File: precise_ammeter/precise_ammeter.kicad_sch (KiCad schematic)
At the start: 0 parts

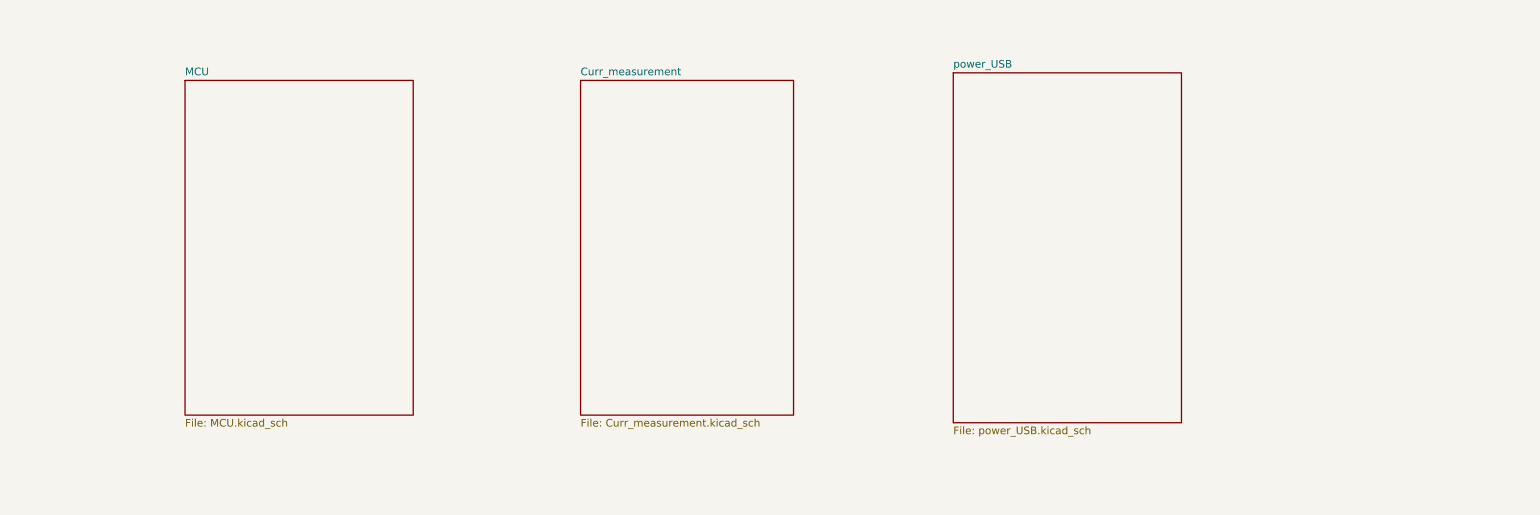
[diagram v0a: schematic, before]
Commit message: Dodano schemat frontend_1
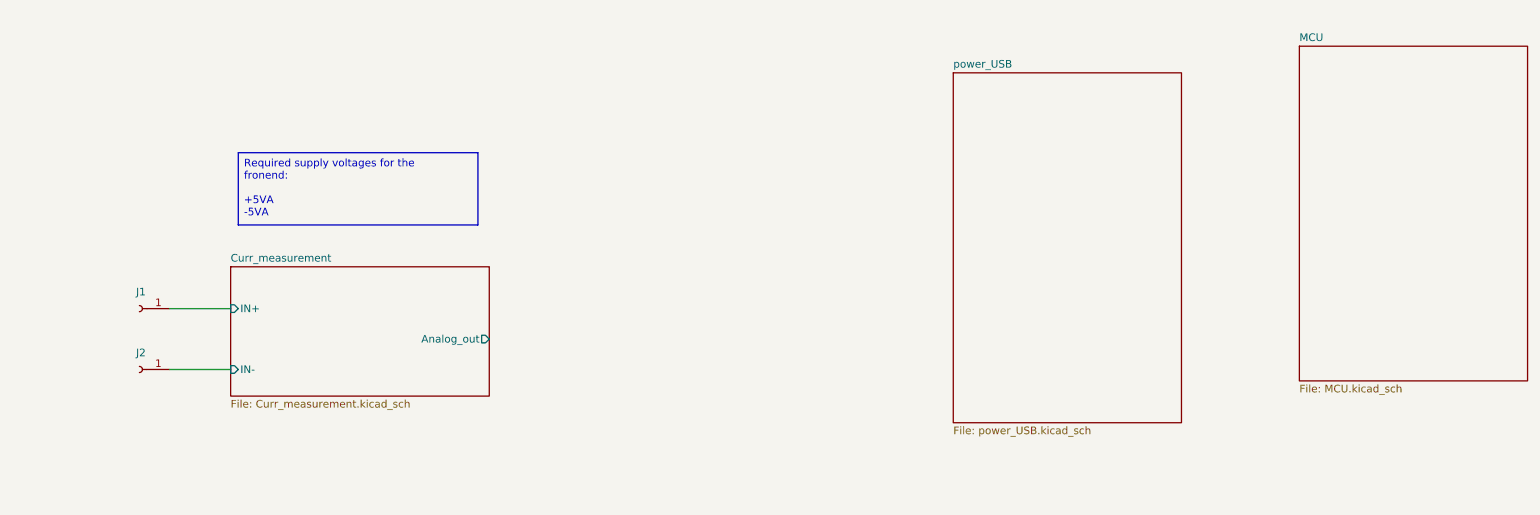
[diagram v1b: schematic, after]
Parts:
- added J1, J2: Conn_01x01_Socket, Connector:Banana_Jack_1Pin, symbol Connector:Conn_01x01_Socket
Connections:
- new net Curr_measurement/IN+: J1.1 (Pin_1)
- new net Curr_measurement/IN-: J2.1 (Pin_1)
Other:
- sheet Curr_measurement ports: added Analog_out, IN+, IN-; removed none
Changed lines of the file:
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@@
 	(generator_version "9.0")
 	(paper "A4")
+	(text_box "Required supply voltages for the fronend:\n\n+5VA\n-5VA"
+		(exclude_from_sim no)
+		(at 57.15 67.945 0)
+		(size 40.005 12.065)
+		(margins 0.9525 0.9525 0.9525 0.9525)
+		(stroke
+			(width 0)
+			(type solid)
+		)
+		(fill
+			(type none)
+		)
+		(effects
+			(font
+				(size 1.27 1.27)
+			)
+			(justify left top)
+		)
+	)
+	(wire
+		(pts
+			(xy 45.72 93.98) (xy 55.88 93.98)
+		)
+		(stroke
+			(width 0)
+			(type default)
+		)
+	)
+	(wire
+		(pts
+			(xy 45.72 104.14) (xy 55.88 104.14)
+		)
+		(stroke
+			(width 0)
+			(type default)
+		)
+	)
+	(symbol
+		(lib_id "Connector:Conn_01x01_Socket")
+		(at 40.64 93.98 180)
+		(unit 1)
+		(exclude_from_sim no)
+		(in_bom yes)
+		(on_board yes)
+		(dnp no)
+		(property "Reference" "J1"
+			(at 40.894 91.186 0)
+			(effects
+				(font
+					(size 1.27 1.27)
+				)
+			)
+		)
+		(property "Value" "Conn_01x01_Socket"
+			(at 41.275 91.44 0)
+			(effects
+				(font
+					(size 1.27 1.27)
+				)
+				(hide yes)
+			)
+		)
+		(property "Footprint" "Connector:Banana_Jack_1Pin"
+			(at 40.64 93.98 0)
+			(effects
+				(font
+					(size 1.27 1.27)
+				)
+				(hide yes)
+			)
+		)
+		(property "Datasheet" "~"
+			(at 40.64 93.98 0)
+			(effects
+				(font
+					(size 1.27 1.27)
+				)
+				(hide yes)
+			)
+		)
+		(property "Description" "Generic connector, single row, 01x01, script generated"
+			(at 40.64 93.98 0)
+			(effects
+				(font
+					(size 1.27 1.27)
+				)
+				(hide yes)
+			)
+		)
+		(pin "1"
+		)
+		(instances
+			(project ""
+				(path "/7da3b652-85ac-4caa-8d8d-9cad461e9c85"
+					(reference "J1")
+					(unit 1)
+				)
+			)
+		)
+	)
+	(symbol
+		(lib_id "Connector:Conn_01x01_Socket")
+		(at 40.64 104.14 180)
+		(unit 1)
+		(exclude_from_sim no)
+		(in_bom yes)
+		(on_board yes)
+		(dnp no)
+		(property "Reference" "J2"
+			(at 40.894 101.346 0)
+			(effects
+				(font
+					(size 1.27 1.27)
+				)
+			)
+		)
+		(property "Value" "Conn_01x01_Socket"
+			(at 41.275 101.6 0)
+			(effects
+				(font
+					(size 1.27 1.27)
+				)
+				(hide yes)
+			)
+		)
+		(property "Footprint" "Connector:Banana_Jack_1Pin"
+			(at 40.64 104.14 0)
+			(effects
+				(font
+					(size 1.27 1.27)
+				)
+				(hide yes)
+			)
+		)
+		(property "Datasheet" "~"
+			(at 40.64 104.14 0)
+			(effects
+				(font
+					(size 1.27 1.27)
+				)
+				(hide yes)
+			)
+		)
+		(property "Description" "Generic connector, single row, 01x01, script generated"
+			(at 40.64 104.14 0)
+			(effects
+				(font
+					(size 1.27 1.27)
+				)
+				(hide yes)
+			)
+		)
+		(pin "1"
+		)
+		(instances
+			(project "precise_ammeter"
+				(path "/7da3b652-85ac-4caa-8d8d-9cad461e9c85"
+					(reference "J2")
+					(unit 1)
+				)
+			)
+		)
+	)
 	(sheet
-		(at 48.26 55.88)
+		(at 234.315 50.165)
 		(size 38.1 55.88)
 		(exclude_from_sim no)
@@
 		)
 		(property "Sheetname" "MCU"
-			(at 48.26 55.1684 0)
+			(at 234.315 49.4534 0)
 			(effects
 				(font
@@
 		)
 		(property "Sheetfile" "MCU.kicad_sch"
-			(at 48.26 112.3446 0)
+			(at 234.315 106.6296 0)
 			(effects
 				(font
@@
 	)
 	(sheet
-		(at 114.3 55.88)
-		(size 35.56 55.88)
+		(at 55.88 86.995)
+		(size 43.18 21.59)
 		(exclude_from_sim no)
 		(in_bom yes)
@@
 		)
 		(property "Sheetname" "Curr_measurement"
-			(at 114.3 55.1684 0)
+			(at 55.88 86.2834 0)
 			(effects
 				(font
@@
 		)
 		(property "Sheetfile" "Curr_measurement.kicad_sch"
-			(at 114.3 112.3446 0)
+			(at 55.88 109.1696 0)
 			(effects
 				(font
@@
 			)
 		)
+		(pin "Analog_out" output
+			(at 99.06 99.06 0)
+			(effects
+				(font
+					(size 1.27 1.27)
+				)
+				(justify right)
+			)
+		)
+		(pin "IN+" input
+			(at 55.88 93.98 180)
+			(effects
+				(font
+					(size 1.27 1.27)
+				)
+				(justify left)
+			)
+		)
+		(pin "IN-" input
+			(at 55.88 104.14 180)
+			(effects
+				(font
+					(size 1.27 1.27)
+				)
+				(justify left)
+			)
+		)

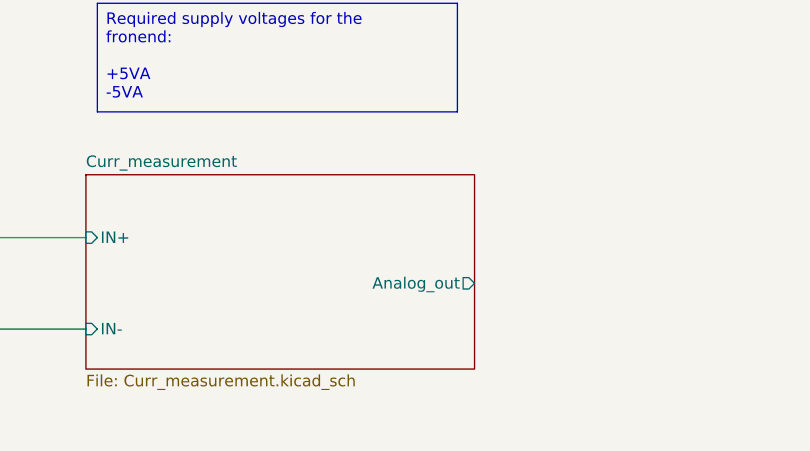
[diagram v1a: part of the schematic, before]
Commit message: Dodano drugi schemat frontendu
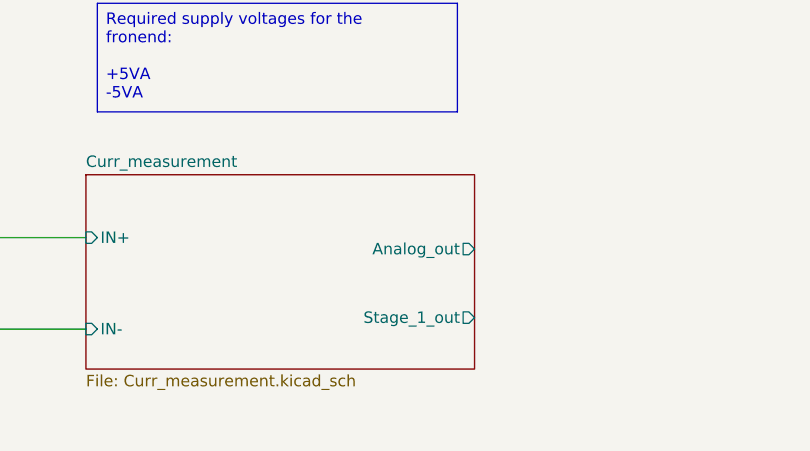
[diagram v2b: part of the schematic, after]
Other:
- sheet Curr_measurement ports: added Stage_1_out; removed none
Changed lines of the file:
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@@
 		)
 		(pin "Analog_out" output
-			(at 99.06 99.06 0)
+			(at 99.06 95.25 0)
 			(effects
 				(font
@@
 			)
 		)
+		(pin "Stage_1_out" output
+			(at 99.06 102.87 0)
+			(effects
+				(font
+					(size 1.27 1.27)
+				)
+				(justify right)
+			)
+		)

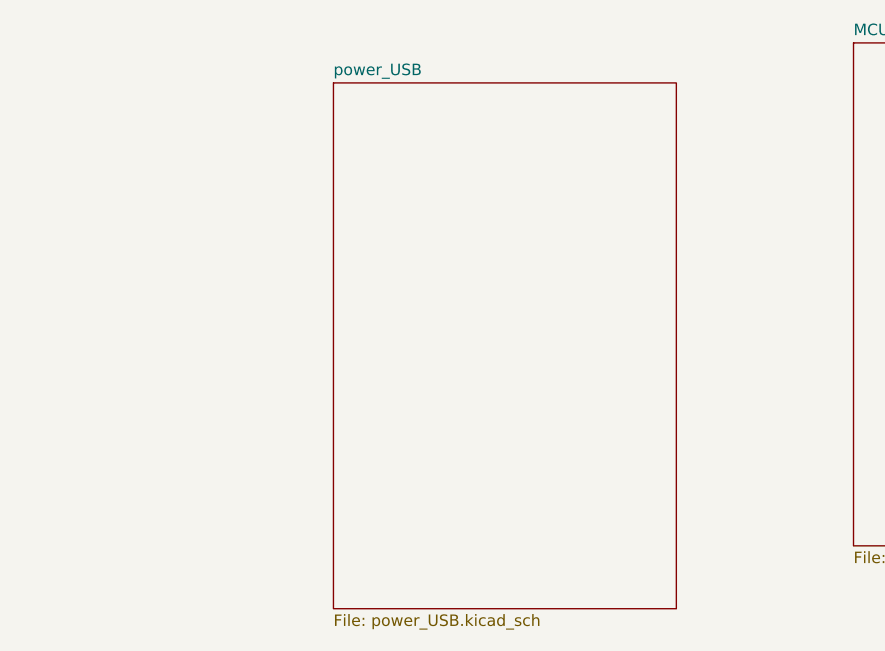
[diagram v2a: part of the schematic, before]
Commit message: Dodano Sekcje zasilanie MCU i wzmacniaczy oraz konektor USB
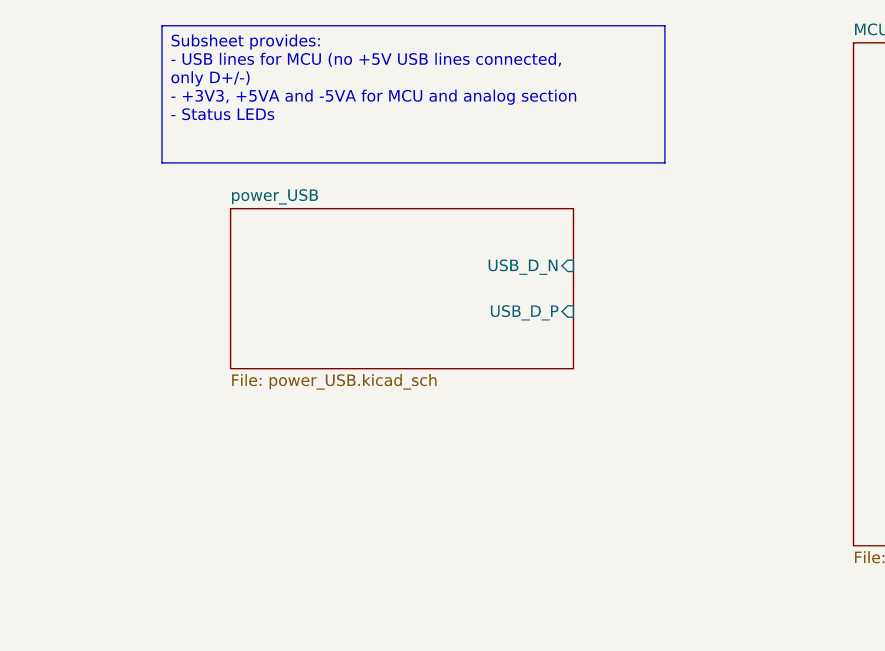
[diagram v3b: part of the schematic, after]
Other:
- sheet power_USB ports: added USB_D_N, USB_D_P; removed none
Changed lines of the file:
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@@
+		)
+	)
+	(text_box "Subsheet provides:\n- USB lines for MCU (no +5V USB lines connected, only D+/-)\n- +3V3, +5VA and -5VA for MCU and analog section\n- Status LEDs"
+		(exclude_from_sim no)
+		(at 157.48 48.26 0)
+		(size 55.88 15.24)
+		(margins 0.9525 0.9525 0.9525 0.9525)
+		(stroke
+			(width 0)
+			(type solid)
+		)
+		(fill
+			(type none)
+		)
+		(effects
+			(font
+				(size 1.27 1.27)
+			)
+			(justify left top)
 		)
 	)
@@
 	)
 	(sheet
-		(at 176.53 54.61)
-		(size 38.1 58.42)
+		(at 165.1 68.58)
+		(size 38.1 17.78)
 		(exclude_from_sim no)
 		(in_bom yes)
@@
 		)
 		(property "Sheetname" "power_USB"
-			(at 176.53 53.8984 0)
+			(at 165.1 67.8684 0)
 			(effects
 				(font
@@
 		)
 		(property "Sheetfile" "power_USB.kicad_sch"
-			(at 176.53 113.6146 0)
+			(at 165.1 86.9446 0)
 			(effects
 				(font
@@
 			)
 		)
+		(pin "USB_D_N" input
+			(at 203.2 74.93 0)
+			(effects
+				(font
+					(size 1.27 1.27)
+				)
+				(justify right)
+			)
+		)
+		(pin "USB_D_P" input
+			(at 203.2 80.01 0)
+			(effects
+				(font
+					(size 1.27 1.27)
+				)
+				(justify right)
+			)
+		)

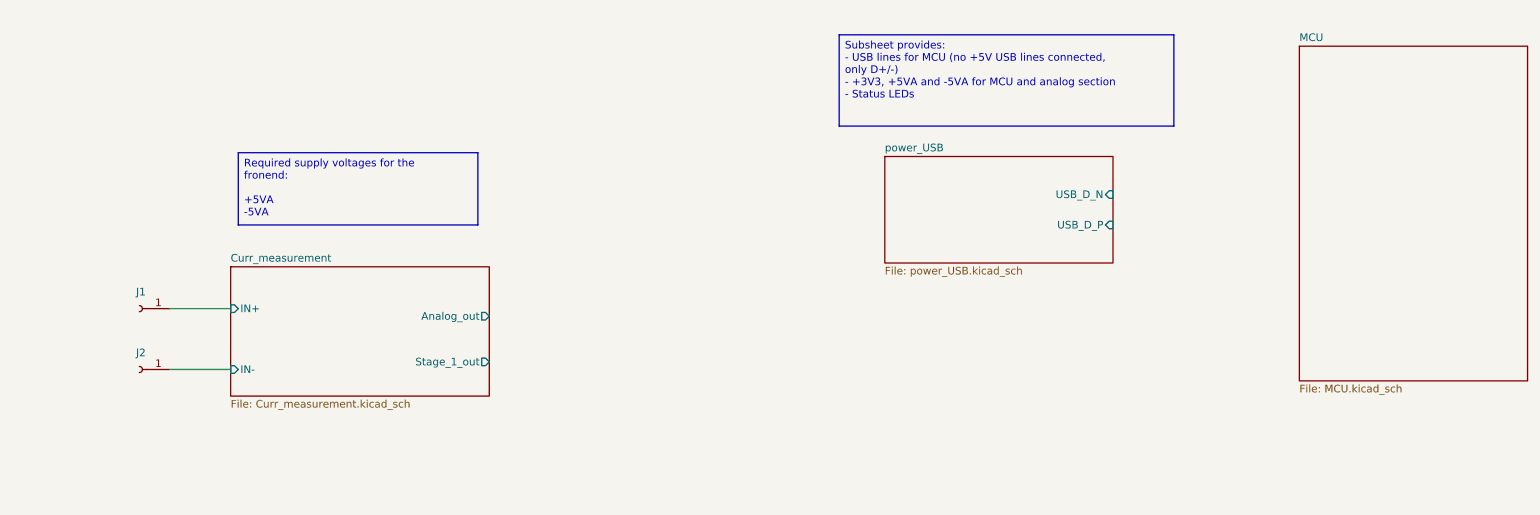
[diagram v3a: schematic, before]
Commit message: added mcu part
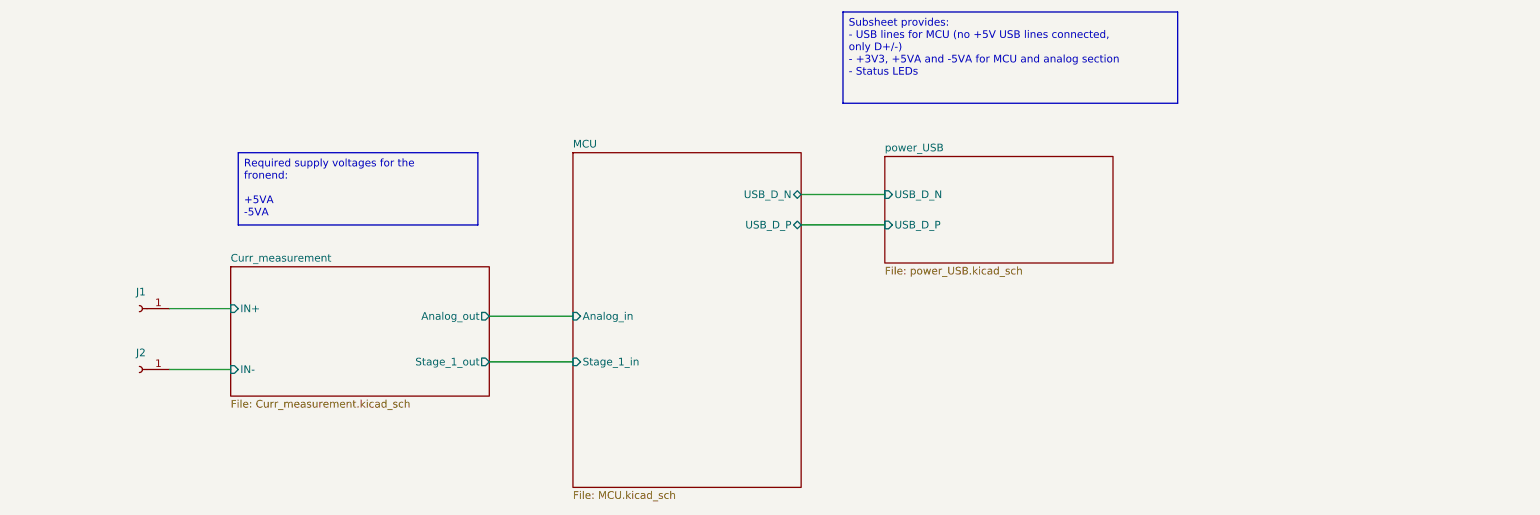
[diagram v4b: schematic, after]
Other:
- sheet MCU ports: added Analog_in, Stage_1_in, USB_D_N, USB_D_P; removed none
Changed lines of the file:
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@@
 	(text_box "Subsheet provides:\n- USB lines for MCU (no +5V USB lines connected, only D+/-)\n- +3V3, +5VA and -5VA for MCU and analog section\n- Status LEDs"
 		(exclude_from_sim no)
-		(at 157.48 48.26 0)
+		(at 158.115 44.45 0)
 		(size 55.88 15.24)
 		(margins 0.9525 0.9525 0.9525 0.9525)
@@
 	(wire
 		(pts
+			(xy 151.13 80.01) (xy 165.1 80.01)
+		)
+		(stroke
+			(width 0)
+			(type default)
+		)
+	)
+	(wire
+		(pts
+			(xy 99.06 95.25) (xy 113.03 95.25)
+		)
+		(stroke
+			(width 0)
+			(type default)
+		)
+	)
+	(wire
+		(pts
+			(xy 99.06 102.87) (xy 113.03 102.87)
+		)
+		(stroke
+			(width 0)
+			(type default)
+		)
+	)
+	(wire
+		(pts
 			(xy 45.72 104.14) (xy 55.88 104.14)
+		)
+		(stroke
+			(width 0)
+			(type default)
+		)
+	)
+	(wire
+		(pts
+			(xy 151.13 74.93) (xy 165.1 74.93)
 		)
 		(stroke
@@
 	)
 	(sheet
-		(at 234.315 50.165)
+		(at 113.03 67.945)
 		(size 38.1 55.88)
 		(exclude_from_sim no)
@@
 		)
 		(property "Sheetname" "MCU"
-			(at 234.315 49.4534 0)
+			(at 113.03 67.2334 0)
 			(effects
 				(font
@@
 		)
 		(property "Sheetfile" "MCU.kicad_sch"
-			(at 234.315 106.6296 0)
+			(at 113.03 124.4096 0)
 			(effects
 				(font
@@
 				)
 				(justify left top)
+			)
+		)
+		(pin "Analog_in" input
+			(at 113.03 95.25 180)
+			(effects
+				(font
+					(size 1.27 1.27)
+				)
+				(justify left)
+			)
+		)
+		(pin "Stage_1_in" input
+			(at 113.03 102.87 180)
+			(effects
+				(font
+					(size 1.27 1.27)
+				)
+				(justify left)
+			)
+		)
+		(pin "USB_D_N" bidirectional
+			(at 151.13 74.93 0)
+			(effects
+				(font
+					(size 1.27 1.27)
+				)
+				(justify right)
+			)
+		)
+		(pin "USB_D_P" bidirectional
+			(at 151.13 80.01 0)
+			(effects
+				(font
+					(size 1.27 1.27)
+				)
+				(justify right)
 			)
 		)
@@
 		)
 		(pin "USB_D_N" input
-			(at 203.2 74.93 0)
-			(effects
-				(font
-					(size 1.27 1.27)
-				)
-				(justify right)
+			(at 165.1 74.93 180)
+			(effects
+				(font
+					(size 1.27 1.27)
+				)
+				(justify left)
 			)
 		)
 		(pin "USB_D_P" input
-			(at 203.2 80.01 0)
-			(effects
-				(font
-					(size 1.27 1.27)
-				)
-				(justify right)
-			)
-		)
+			(at 165.1 80.01 180)
+			(effects
+				(font
+					(size 1.27 1.27)
+				)
+				(justify left)
+			)
+		)

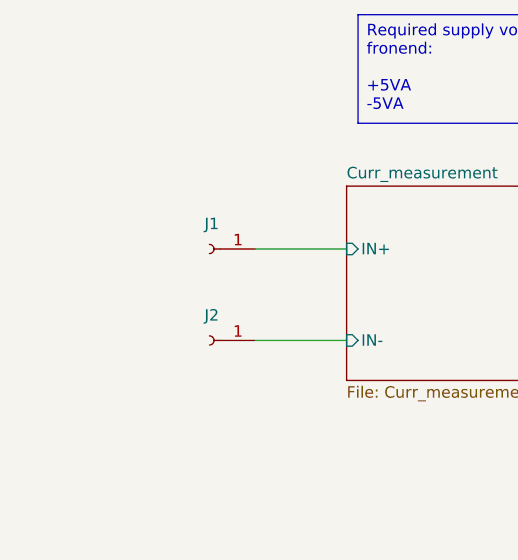
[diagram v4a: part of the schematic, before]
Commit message: added step model for xt30
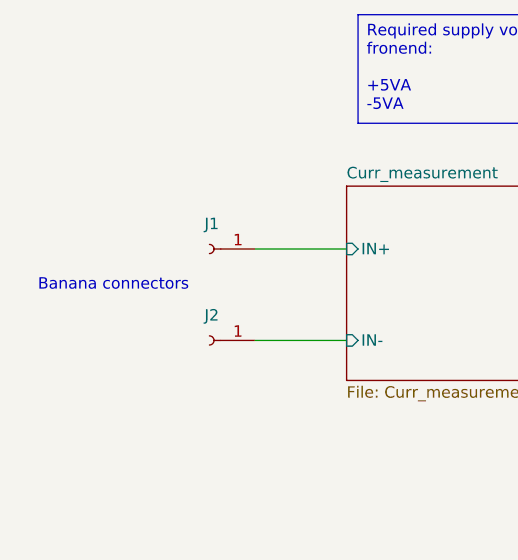
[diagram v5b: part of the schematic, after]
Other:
- note added: "Banana connectors"
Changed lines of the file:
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@@
 	(generator_version "9.0")
 	(paper "A4")
+	(text "Banana connectors"
+		(exclude_from_sim no)
+		(at 29.972 98.044 0)
+		(effects
+			(font
+				(size 1.27 1.27)
+			)
+		)
+	)
 	(text_box "Required supply voltages for the fronend:\n\n+5VA\n-5VA"
 		(exclude_from_sim no)

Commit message: jebane gowno
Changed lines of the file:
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@@
+		)
+	)
+	(label "Stage_IO"
+		(at 102.87 102.87 0)
+		(effects
+			(font
+				(size 1.27 1.27)
+			)
+			(justify left bottom)
+		)
+	)
+	(label "Analog_IO"
+		(at 101.6 95.25 0)
+		(effects
+			(font
+				(size 1.27 1.27)
+			)
+			(justify left bottom)
 		)
 	)
